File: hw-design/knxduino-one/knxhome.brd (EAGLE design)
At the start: 38.9 x 38.9 mm, 47 parts, among them IC1 LDL1117S33, IC2 STM32G071CBT6, IC3 BD9G101, P1 B10B-PH-K, P2 B10B-PH-K, P3 B6B-PH-K, U1 OSCILLATOR5X3-PIN1-INDICATED

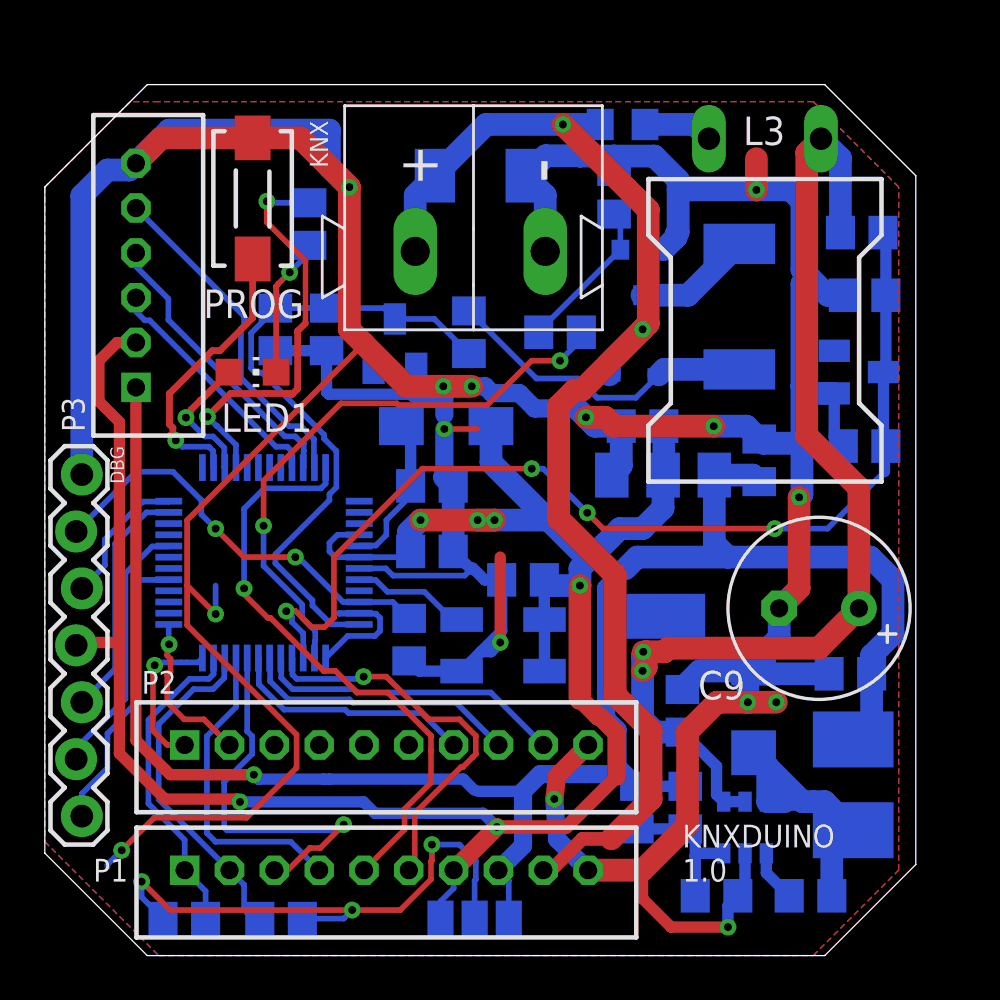
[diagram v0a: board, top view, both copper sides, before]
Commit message: HW files cleanup and image previews
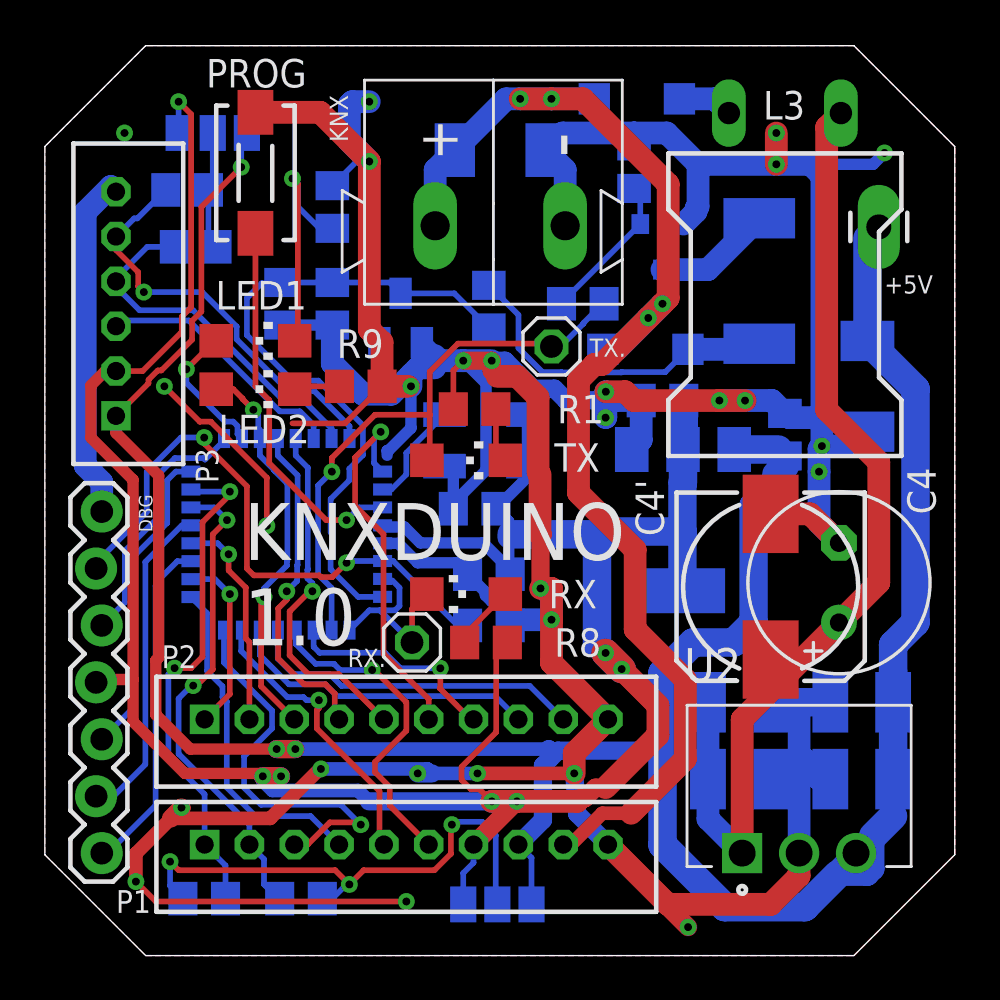
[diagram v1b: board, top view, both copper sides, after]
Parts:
- removed C10*: 10p, rcl:C0805
- removed C12, C13*: 10n, rcl:C0805
- removed C13: 4u7, rcl:C0805
- removed C16: 270n, rcl:C0805
- removed C17: 15nF, rcl:C0805
- removed D100: MBRS1100, diode:SMA
- removed D2*, D4*: 3V3, diode:SOT23
- removed IC2: STM32G071CBT6, stm32g0:LQFP48
- removed IC3: BD9G101, Stefan_selfbus:SOT23-6
- removed L1: FERRITE BEAD, inductor-neosid:SM-B5
- removed L2: 6.8µH, Stefan_selfbus:PIS2812
- removed R25: 2k4, rcl:R0805
- removed R26: 680R, rcl:R0805
- added +5V: (no value), SparkFun-Connectors:1X01_LONGPAD
- added C2', C3': *, rcl:C1210
- added C4: 100uF 50V, rcl:E3,5-8
- added C4': (no value), resistor:153CLV-0810
- added C7: 1u, rcl:C0805
- added D2: SMAJ15CA, diode:DO-214AC
- added D4: 3V3*, diode:SOT23
- added I2CB_U: (no value), jumper:SJ_2
- added IC4: STM32G071KBT6, stm32g0:LQFP32
- added LED2, RX, TX: *, led:CHIPLED_1206
- added R1: 510R*, rcl:R0805
- added R11, R12: 10k, rcl:R0805
- added RX., TX.: (no value), pinhead:1X01
- added U2: VXO7803-500, VXO7803-500:CONV_VXO7803-500
- C10: value 1u -> 10p*
- C2: value 4.7µF/50V -> 10µF/50V; device rcl:C0805 -> rcl:C1210
- C3: value 100n -> 22µ/10V; device rcl:C0805 -> rcl:C1210
- C8: value 22µ/10V -> 4u7
- C9: value 100uF 50V -> 100n; device rcl:E3,5-8 -> rcl:C0805
- D11: device diode:D0805 -> diode:SOD123
- D6: device zetex:SOD323 -> diode:SOD123
- LED1: device led:CHIP-LED0805 -> led:CHIPLED_1206
- R8: value 33k -> 510R*
- R9: value 1k -> 510R*
- moved R8 24.8 mm to (19.7, 14.0), flipped to the top
- moved C3 23.2 mm to (36.4, 7.87)
- moved R9 22.8 mm to (14.1, 25.4), flipped to the top
- moved C10 22.5 mm to (10.5, 29.1), turned to 270 degrees
- moved C9 17.2 mm to (24.0, 29.1), flipped to the bottom, turned to 0 degrees
- moved C8 14.8 mm to (27.6, 24.8), turned to 0 degrees
- moved U1 9.18 mm to (19.7, 23.0)
- moved C2 3.97 mm to (31.0, 7.87), turned to 0 degrees
- moved C5 3.84 mm to (19.2, 19.9)
- moved C6 3.61 mm to (19.8, 14.7), turned to 180 degrees
- moved C1 2.74 mm to (19.8, 17.0), turned to 0 degrees
- moved DBG 1.88 mm to (2.41, 19.8)
- moved P3 1.55 mm to (3.17, 29.1)
- moved KNX 1.45 mm to (20.1, 32.6)
- moved L3 1.45 mm to (33.0, 37.6)
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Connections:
- removed net ADJ: C16.1, IC3.3, R25.1, R26.2
- removed net IOB_PB8: IC2.47, P3.5
- removed net IO_PB0: IC2.19, P2.7
- removed net IO_PB12: IC2.24, P2.1
- removed net IO_PB13: IC2.25, P2.2
- removed net KNX_DC_AN: C13*.1, D2*.3, IC2.15, R8.1, R9.2
- removed net LED2: IC2.40, R10.2
- removed net LX: C17.1, D100.C, IC3.6, L2.P$1
- removed net N$19: C17.2, IC3.1
- removed net N$5: IC2.11, IC2.13
- removed net VDDA: C3.1, IC2.5, L1.2
- new net I2C_PUP1: I2CB_U.2, R11.2, R12.2
- new net IOB_AUX: IC4.30, P3.3
- new net IO_PA4: IC4.11, P2.7
- new net IO_PA8: IC4.18, P2.1
- new net IO_PB3: IC4.27, LED2.A, P2.3
- new net IO_PB4: IC4.28, P2.4
- new net IO_PB5: IC4.29, P2.5
- new net IO_PB9: IC4.1, P2.6
- new net IO_PC6: IC4.20, P2.2
- new net KNX_RX: IC4.7, IC4.9, RX..1, RX.C
- new net N$2: LED1.C, R10.2
- new net N$3: R1.2, TX.C
- new net N$6: LED2.C, R9.2
- net +3V3: now also C8.1, I2CB_U.3, IC1.4, IC4.4, R8.2; no longer C13.1, IC2.4, IC2.6, L1.1
- net BTN: now also IC4.3; no longer IC2.38
- net DRX: now also IC4.21; no longer IC2.32
- net DTX: now also IC4.19; no longer IC2.29
- net GND: now also C2'.1, C3'.1, C3.1, C4'.-, C4.-, C7.2, C8.2, D2.A, D4.1, IC4.5, R1.1, R10.1, U2.2; no longer C10*.2, C13*.2, C13.2, C3.2, C8.1, C9.-, D100.A, D2*.1, D4*.1, IC2.7, IC3.2, R26.1
- net I2CB_SCL: now also IC4.32, P3.5, R11.1; no longer IC2.45, P3.3
- net I2CB_SDA: now also IC4.31, R12.1; no longer IC2.46
- net I2C_SCL: now also IC4.22; no longer IC2.22
- net I2C_SDA: now also IC4.23; no longer IC2.23
- net IO_AN: now also IC4.12; no longer IC2.16
- net IO_DE: now also IC4.16; no longer IC2.20
- net IO_PA6: now also IC4.13; no longer IC2.17
- net IO_PA7: now also IC4.14; no longer IC2.18
- net IO_RX: now also IC4.15; no longer IC2.48
- net IO_TX: now also IC4.17; no longer IC2.21
- net KNX+: now also D6.A; no longer D6.2
- net KNX_DC: now also C2'.2, C4'.+, C4.+, U2.1; no longer C9.+, IC3.4, IC3.5, R8.2
- net KNX_RECT: now also D6.C; no longer D6.1
- net KNX_RX_AN: now also C10.1, D4.3, IC4.8; no longer C10*.1, D4*.3, IC2.12
- net KNX_TX: now also C9.1, IC4.10, TX..1, TX.A; no longer C12.1, IC2.14
- net LED: now also IC4.26; no longer IC2.39
- net N$4: now also R8.1, RX.A; no longer LED1.C, R10.1
- net N$8: now also C9.2; no longer C12.2
- net NRST: now also IC4.6; no longer IC2.10
- net OSC: now also IC4.2; no longer IC2.8
- net SWCLK: now also IC4.25; no longer IC2.36
- net SWDIO: now also IC4.24; no longer IC2.35
- net VCC: now also +5V.1, C3'.2, C3.2, C7.1, D2.C, I2CB_U.1, U2.3; no longer C10.1, C16.2, C8.2, L2.P$2, R25.2
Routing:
- net KNX_DC_AN: track 46.9 -> 0.00 mm, vias 4 -> 0
- net VCC: track 84.4 -> 130.2 mm, vias 1 -> 3
- net +3V3: track 97.4 -> 120.2 mm, vias 6 -> 7
- net LED2: track 18.6 -> 0.00 mm, vias 2 -> 0
- net IO_PB3: track 0.00 -> 17.6 mm, vias 0 -> 2
- net IO_PB9: track 0.00 -> 16.7 mm, vias 0 -> 1
- net IO_PB5: track 0.00 -> 15.9 mm, vias 0 -> 1
- net IOB_PB8: track 15.3 -> 0.00 mm
- net IO_PB4: track 0.00 -> 14.9 mm, vias 0 -> 1
- net LX: track 14.4 -> 0.00 mm
- net IO_RX: track 26.8 -> 13.0 mm
- net GND: track 240.1 -> 252.5 mm, vias 15 -> 27
- net IOB_AUX: track 0.00 -> 11.5 mm
- net IO_PB0: track 11.0 -> 0.00 mm
- net N$2: track 0.00 -> 10.7 mm, vias 0 -> 1
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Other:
- board size 38.9 x 38.9 mm -> 40.6 x 40.6 mm

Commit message: Top and bot. board values presets, values adjusted
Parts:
- LED1: value (none) -> RED
- LED2: value * -> BLUE*
- RX: value * -> GREEN*
- TX: value * -> YELLOW*

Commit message: Bootloader with diff-support and STM32G0 support
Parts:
- D6: value 400mA -> STPS0540Z 400mA
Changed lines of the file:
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@@
 <drawing>
 <settings>
-<setting alwaysvectorfont="yes"/>
+<setting alwaysvectorfont="no"/>
 <setting verticaltext="up"/>
 </settings>
@@
 <attribute name="VALUE" x="28.829" y="36.449" size="1.27" layer="28" rot="MR270"/>
 </element>
-<element name="D6" library="diode" library_urn="urn:adsk.eagle:library:210" package="SOD123" package3d_urn="urn:adsk.eagle:package:43420/1" value="400mA" x="26.797" y="27.051" smashed="yes" rot="MR0">
+<element name="D6" library="diode" library_urn="urn:adsk.eagle:library:210" package="SOD123" package3d_urn="urn:adsk.eagle:package:43420/1" value="STPS0540Z 400mA" x="26.797" y="27.051" smashed="yes" rot="MR0">
 <attribute name="NAME" x="27.443" y="28.212" size="1.016" layer="26" rot="MR0"/>
 <attribute name="VALUE" x="29.983" y="28.421" size="1.016" layer="28" rot="MR0"/>
